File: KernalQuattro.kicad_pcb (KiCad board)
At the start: 2 copper layers, 18.3 x 31 mm, 15 parts, among them CN1 2364, J1 Conn, SW1 DIP Switch, U1 28C256

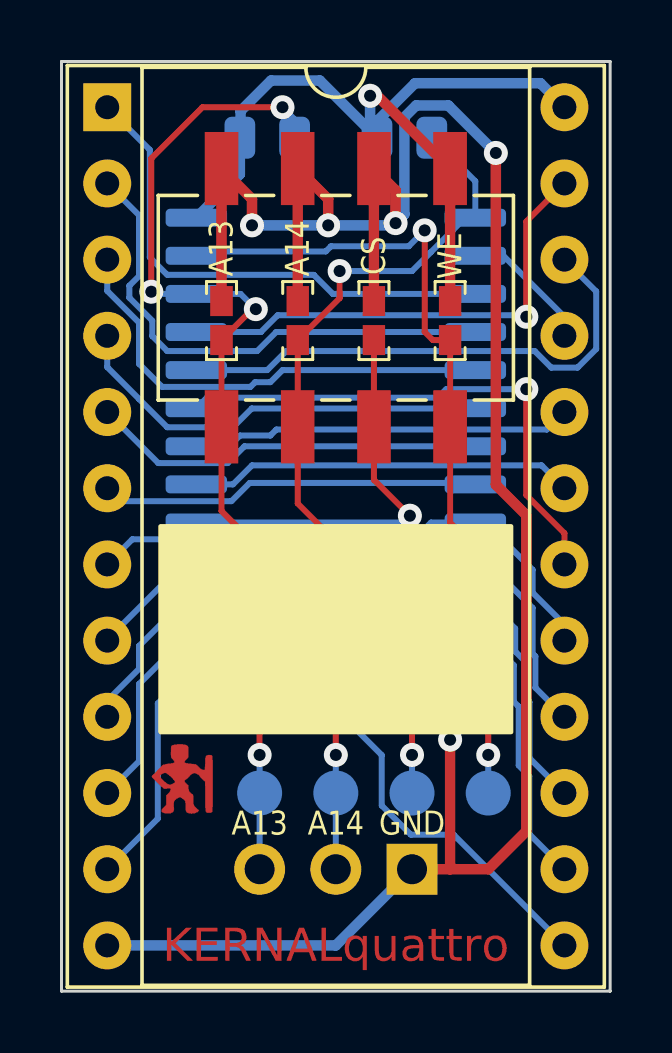
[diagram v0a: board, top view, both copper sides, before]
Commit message: Rounded corners.
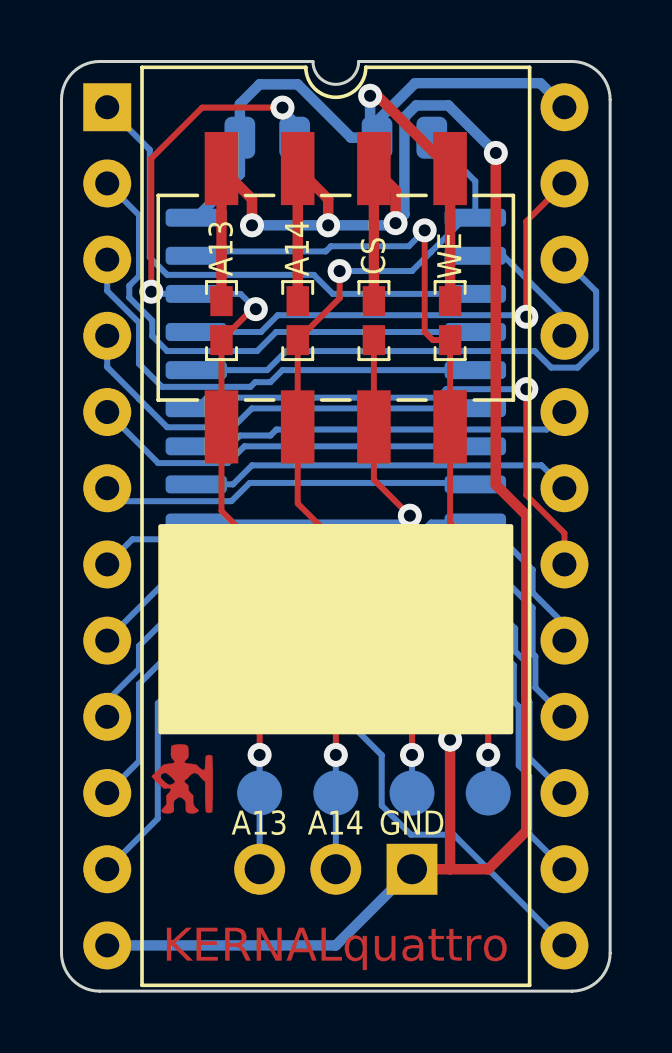
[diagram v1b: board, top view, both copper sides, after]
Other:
- outline, holes or cut-outs redrawn
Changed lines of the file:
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@@
   )
   (paper "A4")
+  (title_block
+    (title "KERNALquattro")
+    (rev "1")
+    (company "www.hackup.net")
+  )
   (layers
     (0 "F.Cu" signal)
@@
       (effects (font (size 1 1) (thickness 0.15)))
     )
-    (fp_line (start 16.57 -1.39) (end -1.33 -1.39) (layer "F.SilkS") (width 0.12))
     (fp_line (start 14.08 -1.33) (end 8.62 -1.33) (layer "F.SilkS") (width 0.12))
     (fp_line (start 6.62 -1.33) (end 1.16 -1.33) (layer "F.SilkS") (width 0.12))
-    (fp_line (start -1.33 29.33) (end 16.57 29.33) (layer "F.SilkS") (width 0.12))
-    (fp_line (start 16.57 29.33) (end 16.57 -1.39) (layer "F.SilkS") (width 0.12))
     (fp_line (start 14.08 29.27) (end 14.08 -1.33) (layer "F.SilkS") (width 0.12))
     (fp_line (start 1.16 -1.33) (end 1.16 29.27) (layer "F.SilkS") (width 0.12))
     (fp_line (start 1.16 29.27) (end 14.08 29.27) (layer "F.SilkS") (width 0.12))
-    (fp_line (start -1.33 -1.39) (end -1.33 29.33) (layer "F.SilkS") (width 0.12))
     (fp_arc (start 8.62 -1.33) (mid 7.62 -0.33) (end 6.62 -1.33) (layer "F.SilkS") (width 0.12))
     (fp_line (start 16.8 29.55) (end 16.8 -1.6) (layer "F.CrtYd") (width 0.05))
@@
     (pad "11" thru_hole oval (at 0 25.4) (size 1.6 1.6) (drill 0.8) (layers *.Cu *.Mask)
       (net 11 "/D2") (pinfunction "D2") (pintype "tri_state"))
-    (pad "12" thru_hole oval locked (at 0 27.94) (size 1.6 1.6) (drill 0.8) (layers *.Cu *.Mask)
+    (pad "12" thru_hole oval (at 0 27.94) (size 1.6 1.6) (drill 0.8) (layers *.Cu *.Mask)
       (net 12 "GND") (pinfunction "GND") (pintype "power_in"))
     (pad "13" thru_hole oval (at 15.24 27.94) (size 1.6 1.6) (drill 0.8) (layers *.Cu *.Mask)
@@
       (xy 124.206 76.454)
     ) (layer "F.SilkS") (width 0.15) (fill solid))
-  (gr_line (start 127.508 60.96) (end 127.508 91.948) (layer "Edge.Cuts") (width 0.1))
-  (gr_line (start 127.508 91.948) (end 109.22 91.948) (layer "Edge.Cuts") (width 0.1))
-  (gr_line (start 109.22 60.96) (end 127.508 60.96) (layer "Edge.Cuts") (width 0.1))
-  (gr_line (start 109.22 91.948) (end 109.22 60.96) (layer "Edge.Cuts") (width 0.1))
+  (gr_arc (start 119.126 60.96) (mid 118.364 61.722) (end 117.602 60.96) (layer "Edge.Cuts") (width 0.1))
+  (gr_arc (start 109.22 62.23) (mid 109.591974 61.331974) (end 110.49 60.96) (layer "Edge.Cuts") (width 0.1))
+  (gr_arc (start 127.508 90.678) (mid 127.136026 91.576026) (end 126.238 91.948) (layer "Edge.Cuts") (width 0.1))
+  (gr_arc (start 110.49 91.948) (mid 109.591974 91.576026) (end 109.22 90.678) (layer "Edge.Cuts") (width 0.1))
+  (gr_line (start 127.508 62.23) (end 127.508 90.678) (layer "Edge.Cuts") (width 0.1))
+  (gr_arc (start 126.238 60.96) (mid 127.136026 61.331974) (end 127.508 62.23) (layer "Edge.Cuts") (width 0.1))
+  (gr_line (start 126.238 60.96) (end 119.126 60.96) (layer "Edge.Cuts") (width 0.1))
+  (gr_line (start 126.238 91.948) (end 110.49 91.948) (layer "Edge.Cuts") (width 0.1))
+  (gr_line (start 110.49 60.96) (end 117.602 60.96) (layer "Edge.Cuts") (width 0.1))
+  (gr_line (start 109.22 90.678) (end 109.22 62.23) (layer "Edge.Cuts") (width 0.1))
   (gr_text "KERNALquattro" (at 118.364 90.424) (layer "F.Cu")
     (effects (font (size 1.1 1.1) (thickness 0.25)))
@@
   (segment (start 122.174 64.529) (end 119.748 62.103) (width 0.35) (layer "F.Cu") (net 23))
   (via (at 119.507 62.103) (size 0.8) (drill 0.4) (layers "F.Cu" "B.Cu") (net 23))
-  (segment (start 117.8325 61.595) (end 119.7375 63.5) (width 0.35) (layer "B.Cu") (net 23))
-  (segment (start 115.189 62.611) (end 116.205 61.595) (width 0.35) (layer "B.Cu") (net 23))
   (segment (start 125.184001 61.684001) (end 121.005669 61.684001) (width 0.35) (layer "B.Cu") (net 23))
   (segment (start 119.7375 62.95217) (end 119.7375 63.5) (width 0.35) (layer "B.Cu") (net 23))
   (segment (start 125.984 62.484) (end 125.184001 61.684001) (width 0.35) (layer "B.Cu") (net 23))
   (segment (start 121.005669 61.684001) (end 119.7375 62.95217) (width 0.35) (layer "B.Cu") (net 23))
-  (segment (start 116.205 61.595) (end 117.8325 61.595) (width 0.35) (layer "B.Cu") (net 23))
-  (segment (start 115.1655 63.5) (end 115.189 63.4765) (width 0.35) (layer "B.Cu") (net 23))
+  (segment (start 115.824 61.722) (end 117.094 61.722) (width 0.35) (layer "B.Cu") (net 23))
+  (segment (start 117.094 61.722) (end 118.872 63.5) (width 0.35) (layer "B.Cu") (net 23))
+  (segment (start 115.1655 63.5) (end 115.1655 62.3805) (width 0.35) (layer "B.Cu") (net 23))
   (segment (start 119.507 62.103) (end 119.507 63.2695) (width 0.35) (layer "B.Cu") (net 23))
   (segment (start 115.1655 64.7155) (end 113.714 66.167) (width 0.35) (layer "B.Cu") (net 23))
   (segment (start 119.507 63.2695) (end 119.7375 63.5) (width 0.35) (layer "B.Cu") (net 23))
-  (segment (start 115.189 63.4765) (end 115.189 62.611) (width 0.35) (layer "B.Cu") (net 23))
   (segment (start 115.1655 63.5) (end 115.1655 64.7155) (width 0.35) (layer "B.Cu") (net 23))
+  (segment (start 118.872 63.5) (end 119.7375 63.5) (width 0.35) (layer "B.Cu") (net 23))
+  (segment (start 115.1655 62.3805) (end 115.824 61.722) (width 0.35) (layer "B.Cu") (net 23))
   (segment (start 118.491 67.945) (end 118.491 68.849) (width 0.2) (layer "F.Cu") (net 24))
   (segment (start 118.364 76.962) (end 117.094 75.692) (width 0.2) (layer "F.Cu") (net 24))
@@
   (segment (start 118.364 85.344) (end 118.364 84.074) (width 0.2) (layer "B.Cu") (net 24))
   (segment (start 123.014 66.167) (end 123.014 64.9515) (width 0.2) (layer "B.Cu") (net 24))
-  (segment (start 113.919 62.484) (end 116.586 62.484) (width 0.2) (layer "F.Cu") (net 25))
+  (segment (start 113.9065 62.4965) (end 116.586 62.4965) (width 0.2) (layer "F.Cu") (net 25))
+  (segment (start 112.213744 64.189256) (end 113.9065 62.4965) (width 0.2) (layer "F.Cu") (net 25))
   (segment (start 114.554 70.246) (end 114.554 73.139) (width 0.2) (layer "F.Cu") (net 25))
-  (segment (start 112.213744 68.634256) (end 112.213744 64.189256) (width 0.2) (layer "F.Cu") (net 25))
   (segment (start 115.697 69.215) (end 115.585 69.215) (width 0.2) (layer "F.Cu") (net 25))
   (segment (start 115.824 77.216) (end 114.554 75.946) (width 0.2) (layer "F.Cu") (net 25))
   (segment (start 115.585 69.215) (end 114.554 70.246) (width 0.2) (layer "F.Cu") (net 25))
-  (segment (start 112.213744 64.189256) (end 113.919 62.484) (width 0.2) (layer "F.Cu") (net 25))
+  (segment (start 112.213744 68.634256) (end 112.213744 64.189256) (width 0.2) (layer "F.Cu") (net 25))
   (segment (start 114.554 75.946) (end 114.554 73.139) (width 0.2) (layer "F.Cu") (net 25))
   (segment (start 115.824 84.074) (end 115.824 77.216) (width 0.2) (layer "F.Cu") (net 25))
   (via (at 112.213744 68.634256) (size 0.8) (drill 0.4) (layers "F.Cu" "B.Cu") (net 25))
   (via (at 115.697 69.215) (size 0.8) (drill 0.4) (layers "F.Cu" "B.Cu") (net 25))
-  (via (at 116.586 62.484) (size 0.8) (drill 0.4) (layers "F.Cu" "B.Cu") (net 25))
+  (via (at 116.586 62.4965) (size 0.8) (drill 0.4) (layers "F.Cu" "B.Cu") (net 25))
   (via (at 115.824 84.074) (size 0.8) (drill 0.4) (layers "F.Cu" "B.Cu") (net 25))
   (segment (start 115.189 68.707) (end 115.697 69.215) (width 0.2) (layer "B.Cu") (net 25))
-  (segment (start 116.9905 62.8885) (end 116.9905 63.5) (width 0.2) (layer "B.Cu") (net 25))
+  (segment (start 116.9905 63.5) (end 116.9905 62.901) (width 0.2) (layer "B.Cu") (net 25))
   (segment (start 113.714 68.707) (end 112.286488 68.707) (width 0.2) (layer "B.Cu") (net 25))
-  (segment (start 116.586 62.484) (end 116.9905 62.8885) (width 0.2) (layer "B.Cu") (net 25))
+  (segment (start 116.9905 62.901) (end 116.586 62.4965) (width 0.2) (layer "B.Cu") (net 25))
   (segment (start 113.714 68.707) (end 115.189 68.707) (width 0.2) (layer "B.Cu") (net 25))
   (segment (start 115.824 85.344) (end 115.824 84.074) (width 0.2) (layer "B.Cu") (net 25))

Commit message: Work in progress.
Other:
- board text added: "github.com/hackup/ KERNALquattro Rev.1"
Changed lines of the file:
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@@
     (pad "3" thru_hole oval (at 0 5.08 270) (size 1.7 1.7) (drill 1) (layers *.Cu *.Mask)
       (net 25 "/A13") (pinfunction "Pin_3") (pintype "passive"))
-    (model "${KICAD6_3DMODEL_DIR}/Connector_PinHeader_2.54mm.3dshapes/PinHeader_1x03_P2.54mm_Horizontal.wrl"
+    (model "${KICAD6_3DMODEL_DIR}/Connector_PinHeader_2.54mm.3dshapes/PinHeader_1x03_P2.54mm_Horizontal.wrl" hide
       (offset (xyz 0 0 0))
       (scale (xyz 1 1 1))
@@
     (pad "24" thru_hole oval (at 15.24 0) (size 1.6 1.6) (drill 0.8) (layers *.Cu *.Mask)
       (net 23 "+5V") (pinfunction "VCC") (pintype "power_in"))
-    (model "${KICAD6_3DMODEL_DIR}/Package_DIP.3dshapes/DIP-24_W15.24mm_Socket.wrl"
-      (offset (xyz 0 0 0))
-      (scale (xyz 1 1 1))
-      (rotate (xyz 0 0 0))
+    (model "${KICAD6_3DMODEL_DIR}/Connector_PinHeader_2.54mm.3dshapes/PinHeader_1x12_P2.54mm_Vertical.wrl"
+      (offset (xyz 0 0 -1.6))
+      (scale (xyz 1 1 1))
+      (rotate (xyz 0 180 0))
+    )
+    (model "${KICAD6_3DMODEL_DIR}/Connector_PinHeader_2.54mm.3dshapes/PinHeader_1x12_P2.54mm_Vertical.wrl"
+      (offset (xyz 15.24 0 -1.6))
+      (scale (xyz 1 1 1))
+      (rotate (xyz 0 180 0))
     )
   )
@@
     (effects (font (size 1.1 1.1) (thickness 0.25)))
   )
+  (gr_text "github.com/hackup/\nKERNALquattro Rev.1" (at 123.698 90.17) (layer "B.SilkS")
+    (effects (font (size 0.7 0.7) (thickness 0.1)) (justify left mirror))
+  )
   (gr_text "GND" (at 120.904 86.36) (layer "F.SilkS")

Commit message: Work in progress.
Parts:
- added G***: LOGO, Library:quattro, F.Cu at (118.5, 91.1)
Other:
- board text added: "KERNAL"
- board text removed: "KERNALquattro"
